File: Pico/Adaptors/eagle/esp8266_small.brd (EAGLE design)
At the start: 17.4 x 15.2 mm, 4 parts, among them IC1 LD117AS33TR

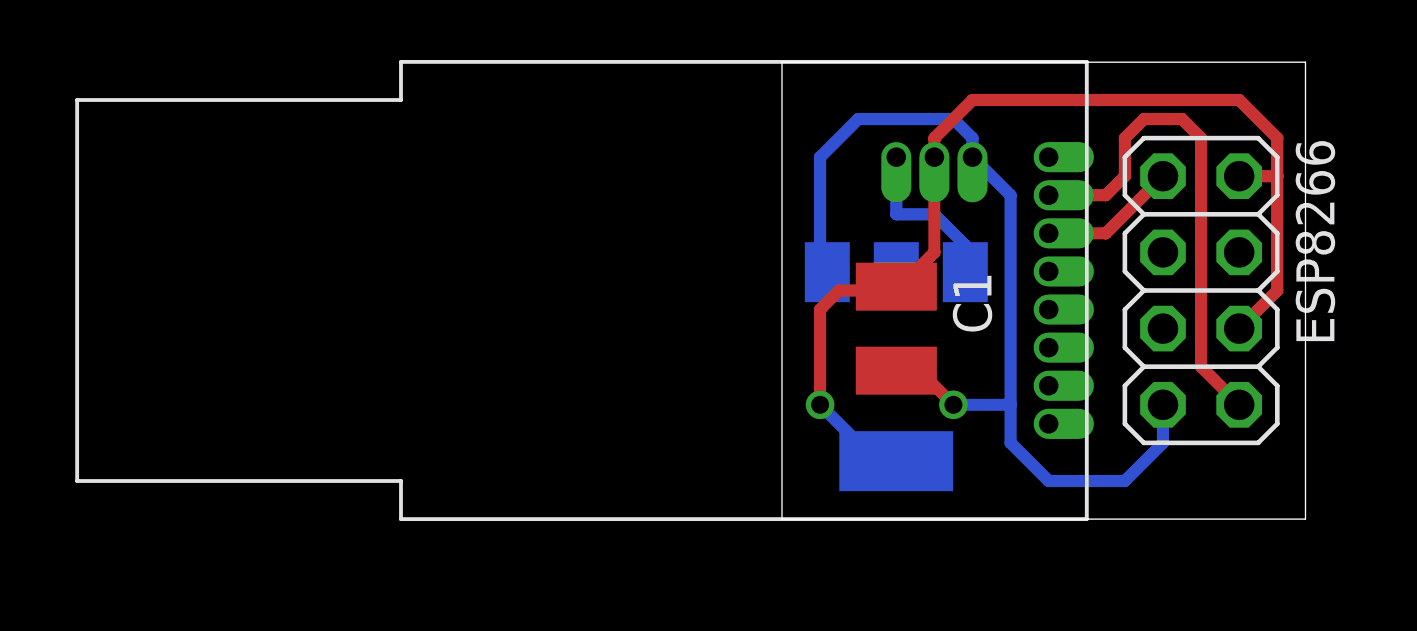
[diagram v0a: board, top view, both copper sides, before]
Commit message: arduino adaptor
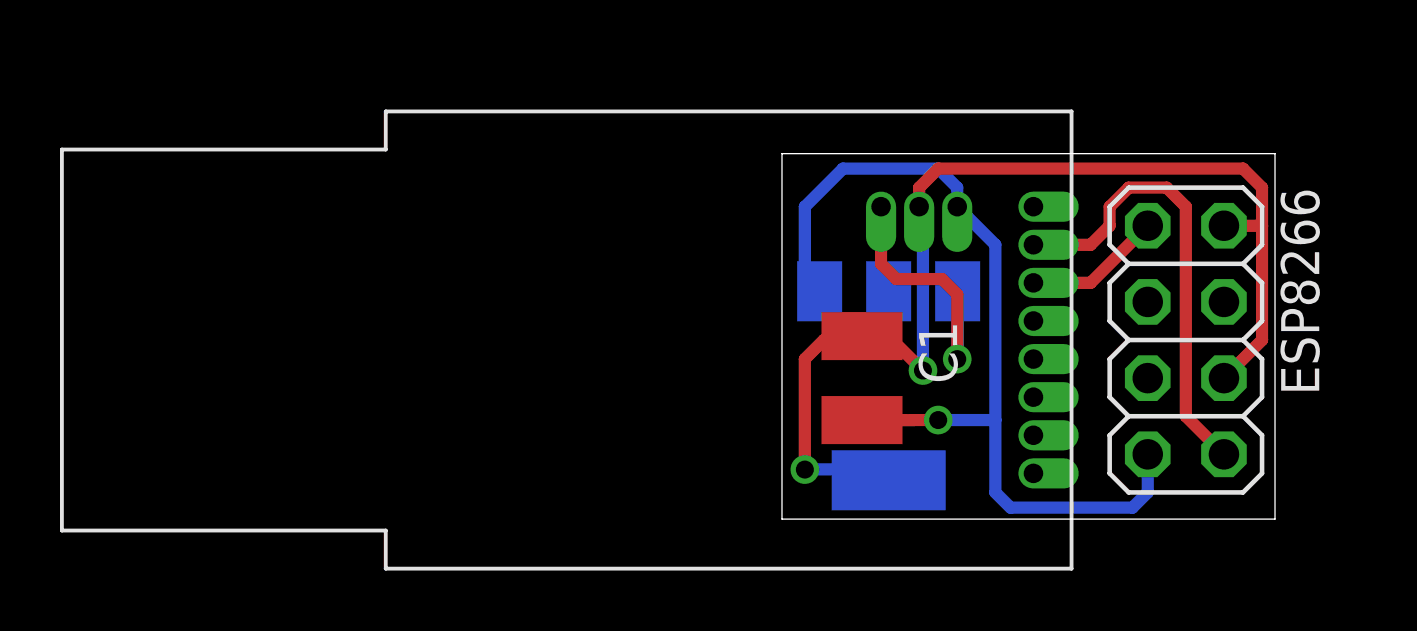
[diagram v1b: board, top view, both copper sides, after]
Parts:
- moved C1 2.01 mm to (2.67, 4.70)
- moved ESP8266 1.73 mm to (13.5, 5.97)
- moved U$1 1.73 mm to (2.03, 5.97)
- moved IC1 0.68 mm to (3.56, 4.45)
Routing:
- net N$1: track 5.53 -> 9.29 mm, vias 0 -> 1
- net VCC: track 35.5 -> 38.4 mm, vias 1 -> 2
- net ESP_TX: track 16.6 -> 15.3 mm
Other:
- board size 17.4 x 15.2 mm -> 16.4 x 12.2 mm
